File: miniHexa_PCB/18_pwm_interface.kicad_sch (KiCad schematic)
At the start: 28 parts, among them U5 PCA9685BS

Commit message: update
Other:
- moved on the sheet: R21, U5

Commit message: layout phase pcb
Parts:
- removed R13, R14, R15, R16, R17, R18: 1k, Resistor_SMD:R_0805_2012Metric, symbol Device:R
- R20, R21: footprint Resistor_SMD:R_0805_2012Metric -> Resistor_SMD:R_0402_1005Metric
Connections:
- net SERVO13: now also Servo13.3 (Pin_3)
- net SERVO14: now also Servo14.3 (Pin_3)
- net SERVO15: now also Servo15.3 (Pin_3)
- net SERVO16: now also Servo16.3 (Pin_3)
- net SERVO17: now also Servo17.3 (Pin_3)
- net SERVO18: now also Servo18.3 (Pin_3)

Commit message: layout done
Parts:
- R19: footprint Resistor_SMD:R_0805_2012Metric -> Resistor_SMD:R_0402_1005Metric
- R21: value R -> 10k
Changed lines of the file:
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@@
 			)
 		)
-		(property "Value" "R"
+		(property "Value" "10k"
 			(at 193.04 97.7899 0)
 			(show_name no)
@@
 			)
 		)
-		(property "Footprint" "Resistor_SMD:R_0805_2012Metric"
+		(property "Footprint" "Resistor_SMD:R_0402_1005Metric"
 			(at 176.022 90.17 90)
 			(hide yes)

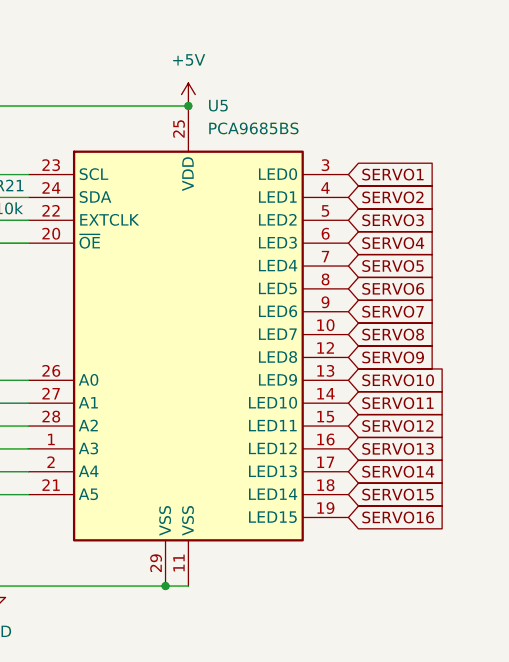
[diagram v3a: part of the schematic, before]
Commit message: routing complete with drc
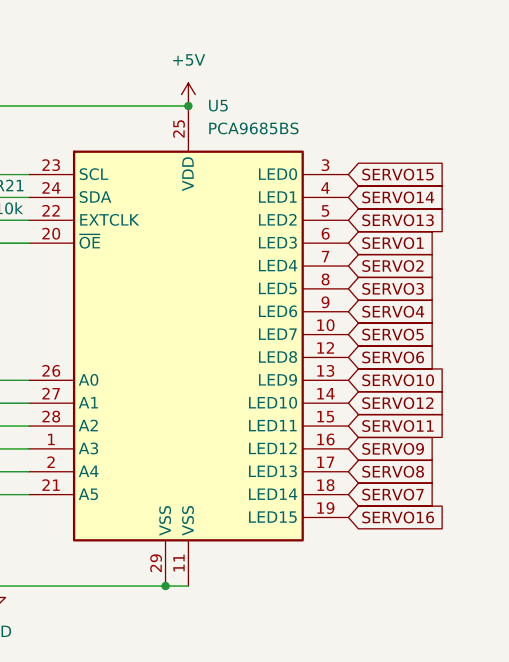
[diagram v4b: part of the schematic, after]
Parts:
- R19: footprint Resistor_SMD:R_0402_1005Metric -> Resistor_SMD:R_0603_1608Metric
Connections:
- net SERVO1: now also U5.6 (LED3); no longer U5.3 (LED0)
- net SERVO11: now also U5.15 (LED11); no longer U5.14 (LED10)
- net SERVO12: now also U5.14 (LED10); no longer U5.15 (LED11)
- net SERVO13: now also U5.5 (LED2); no longer U5.16 (LED12)
- net SERVO14: now also U5.4 (LED1); no longer U5.17 (LED13)
- net SERVO15: now also U5.3 (LED0); no longer U5.18 (LED14)
- net SERVO2: now also U5.7 (LED4); no longer U5.4 (LED1)
- net SERVO3: now also U5.8 (LED5); no longer U5.5 (LED2)
- net SERVO4: now also U5.9 (LED6); no longer U5.6 (LED3)
- net SERVO5: now also U5.10 (LED7); no longer U5.7 (LED4)
- net SERVO6: now also U5.12 (LED8); no longer U5.8 (LED5)
- net SERVO7: now also U5.18 (LED14); no longer U5.9 (LED6)
- net SERVO8: now also U5.17 (LED13); no longer U5.10 (LED7)
- net SERVO9: now also U5.16 (LED12); no longer U5.12 (LED8)

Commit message: start of version 2.0
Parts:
- removed R19: R, Resistor_SMD:R_0603_1608Metric, symbol Device:R
- removed R20: R, Resistor_SMD:R_0402_1005Metric, symbol Device:R
- removed R21: 10k, Resistor_SMD:R_0402_1005Metric, symbol Device:R
- removed Servo1, Servo10, Servo11, Servo12, Servo13, Servo14, Servo15, Servo16, Servo17, Servo18, Servo2, Servo3, Servo4, Servo5, Servo6, Servo7, Servo8, Servo9: Conn_01x03_Pin, Connector_JST:JST_XH_B3B-XH-AM_1x03_P2.50mm_Vertical, symbol Connector:Conn_01x03_Pin
- removed U5: PCA9685BS, Package_DFN_QFN:QFN-28-1EP_6x6mm_P0.65mm_EP4.25x4.25mm, symbol Driver_LED:PCA9685BS
- added J1: FR_L, Connector_JST:JST_XH_S3B-XH-A-1_1x03_P2.50mm_Horizontal, symbol Connector:Conn_01x03_Socket
- added J3: FR_R, Connector_JST:JST_XH_S3B-XH-A-1_1x03_P2.50mm_Horizontal, symbol Connector:Conn_01x03_Socket
- added J4: MID_L, Connector_JST:JST_XH_S3B-XH-A-1_1x03_P2.50mm_Horizontal, symbol Connector:Conn_01x03_Socket
- added J5: MID_R, Connector_JST:JST_XH_S3B-XH-A-1_1x03_P2.50mm_Horizontal, symbol Connector:Conn_01x03_Socket
- added J6: BK_L, Connector_JST:JST_XH_S3B-XH-A-1_1x03_P2.50mm_Horizontal, symbol Connector:Conn_01x03_Socket
- added J7: BK_R, Connector_JST:JST_XH_S3B-XH-A-1_1x03_P2.50mm_Horizontal, symbol Connector:Conn_01x03_Socket
- added Q1: BC807, Package_TO_SOT_SMD:SOT-23, symbol Transistor_BJT:BC807
- added R4, R5: 10K, symbol Device:R
- added U2: SN74LVC1G125DBV, Package_TO_SOT_SMD:SOT-23-5, symbol 74xGxx:SN74LVC1G125DBV
- added U5: SN74LVC1G126DBV, Package_TO_SOT_SMD:SOT-23-5, symbol 74xGxx:SN74LVC1G125DBV
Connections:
- net +5V: now also J1.2 (Pin_2), J3.2 (Pin_2), J4.2 (Pin_2), J5.2 (Pin_2), J6.2 (Pin_2), J7.2 (Pin_2)
- net GND: now also J1.3 (Pin_3), J3.3 (Pin_3), J4.3 (Pin_3), J5.3 (Pin_3), J6.3 (Pin_3), J7.3 (Pin_3), R5.2, U2.3 (GND), U5.3 (GND)
- new net: R4.2, R5.1
- new net +3.3V: Q1.2 (E), U2.5 (VCC), U5.5 (VCC)
- new net RX: U5.2
- new net SERVO_DATA: J1.1 (Pin_1), J3.1 (Pin_1), J4.1 (Pin_1), J5.1 (Pin_1), J6.1 (Pin_1), J7.1 (Pin_1), U2.4, U5.4
- new net TX: Q1.1 (B), U2.2
- new net TX_EN: Q1.3 (C), R4.1, U2.1, U5.1 (Input)

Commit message: mega update
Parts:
- J1, J3, J4, J5, J6, J7: footprint Connector_JST:JST_XH_S3B-XH-A-1_1x03_P2.50mm_Horizontal -> Connector_JST:JST_XH_B3B-XH-A_1x03_P2.50mm_Vertical
- R4, R5: footprint (none) -> Resistor_SMD:R_0402_1005Metric
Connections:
- net RX renamed SERVO_RX
- net TX renamed SERVO_TX
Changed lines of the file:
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@@
 		)
 	)
-	(global_label "TX"
+	(global_label "SERVO_TX"
 		(shape input)
 		(at 35.56 46.99 180)
@@
 		)
 		(property "Intersheetrefs" "${INTERSHEET_REFS}"
-			(at 30.3977 46.99 0)
+			(at 23.3825 46.99 0)
 			(hide yes)
 			(show_name no)
@@
 		)
 	)
+	(global_label "SERVO_TX"
+		(shape input)
+		(at 105.41 63.5 0)
+		(fields_autoplaced yes)
+		(effects
+			(font
+				(size 1.27 1.27)
+			)
+			(justify left)
+		)
+		(property "Intersheetrefs" "${INTERSHEET_REFS}"
+			(at 117.5875 63.5 0)
+			(hide yes)
+			(show_name no)
+			(do_not_autoplace no)
+			(effects
+				(font
+					(size 1.27 1.27)
+				)
+				(justify left)
+			)
+		)
+	)
 	(global_label "TX_EN"
 		(shape input)
@@
 		)
 	)
-	(global_label "RX"
+	(global_label "SERVO_RX"
 		(shape input)
 		(at 35.56 92.71 180)
@@
 		)
 		(property "Intersheetrefs" "${INTERSHEET_REFS}"
-			(at 30.0953 92.71 0)
+			(at 23.0801 92.71 0)
 			(hide yes)
 			(show_name no)
@@
 		)
 	)
-	(global_label "TX"
+	(global_label "SERVO_DATA"
 		(shape input)
-		(at 105.41 63.5 0)
+		(at 172.72 40.64 180)
 		(fields_autoplaced yes)
 		(effects
@@
 				(size 1.27 1.27)
 			)
-			(justify left)
-		)
-		(property "Intersheetrefs" "${INTERSHEET_REFS}"
-			(at 110.5723 63.5 0)
-			(hide yes)
-			(show_name no)
-			(do_not_autoplace no)
-			(effects
-				(font
-					(size 1.27 1.27)
-				)
-				(justify left)
-			)
-		)
-	)
-	(global_label "SERVO_DATA"
-		(shape input)
-		(at 172.72 40.64 180)
-		(fields_autoplaced yes)
-		(effects
-			(font
-				(size 1.27 1.27)
-			)
 			(justify right)
 		)
@@
 			)
 		)
-		(property "Footprint" ""
+		(property "Footprint" "Resistor_SMD:R_0402_1005Metric"
 			(at 71.12 71.882 90)
 			(hide yes)
@@
 			)
 		)
-		(property "Footprint" "Connector_JST:JST_XH_S3B-XH-A-1_1x03_P2.50mm_Horizontal"
+		(property "Footprint" "Connector_JST:JST_XH_B3B-XH-A_1x03_P2.50mm_Vertical"
 			(at 193.04 43.18 0)
 			(hide yes)
@@
 			)
 		)
-		(property "Footprint" "Connector_JST:JST_XH_S3B-XH-A-1_1x03_P2.50mm_Horizontal"
+		(property "Footprint" "Connector_JST:JST_XH_B3B-XH-A_1x03_P2.50mm_Vertical"
 			(at 226.06 43.18 0)
 			(hide yes)
@@
 			)
 		)
-		(property "Footprint" "Connector_JST:JST_XH_S3B-XH-A-1_1x03_P2.50mm_Horizontal"
+		(property "Footprint" "Connector_JST:JST_XH_B3B-XH-A_1x03_P2.50mm_Vertical"
 			(at 240.03 43.18 0)
 			(hide yes)
@@
 			)
 		)
-		(property "Footprint" "Connector_JST:JST_XH_S3B-XH-A-1_1x03_P2.50mm_Horizontal"
+		(property "Footprint" "Connector_JST:JST_XH_B3B-XH-A_1x03_P2.50mm_Vertical"
 			(at 177.8 43.18 0)
 			(hide yes)
@@
 			)
 		)
-		(property "Footprint" "Connector_JST:JST_XH_S3B-XH-A-1_1x03_P2.50mm_Horizontal"
+		(property "Footprint" "Connector_JST:JST_XH_B3B-XH-A_1x03_P2.50mm_Vertical"
 			(at 254 43.18 0)
 			(hide yes)
@@
 			)
 		)
-		(property "Footprint" "Connector_JST:JST_XH_S3B-XH-A-1_1x03_P2.50mm_Horizontal"
+		(property "Footprint" "Connector_JST:JST_XH_B3B-XH-A_1x03_P2.50mm_Vertical"
 			(at 208.28 43.18 0)
 			(hide yes)
@@
 			)
 		)
-		(property "Footprint" ""
+		(property "Footprint" "Resistor_SMD:R_0402_1005Metric"
 			(at 83.82 71.882 90)
 			(hide yes)
